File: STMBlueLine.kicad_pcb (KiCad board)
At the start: 2 copper layers, 22 x 42 mm, 80 parts, among them J1 Micro_SD_Card_Det1, J2 USB_C_Receptacle_USB2.0_14P, J3 Conn_01x04_Pin, SW1 SW_Push, SW2 SW_Push, U1 STM32H750VBTx, U2 TLV320AIC3104IRHBR, U3 TLV320AIC3104IRHBR, U4 LD1117S33TR_SOT223, U5 USBLC6-2SC6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

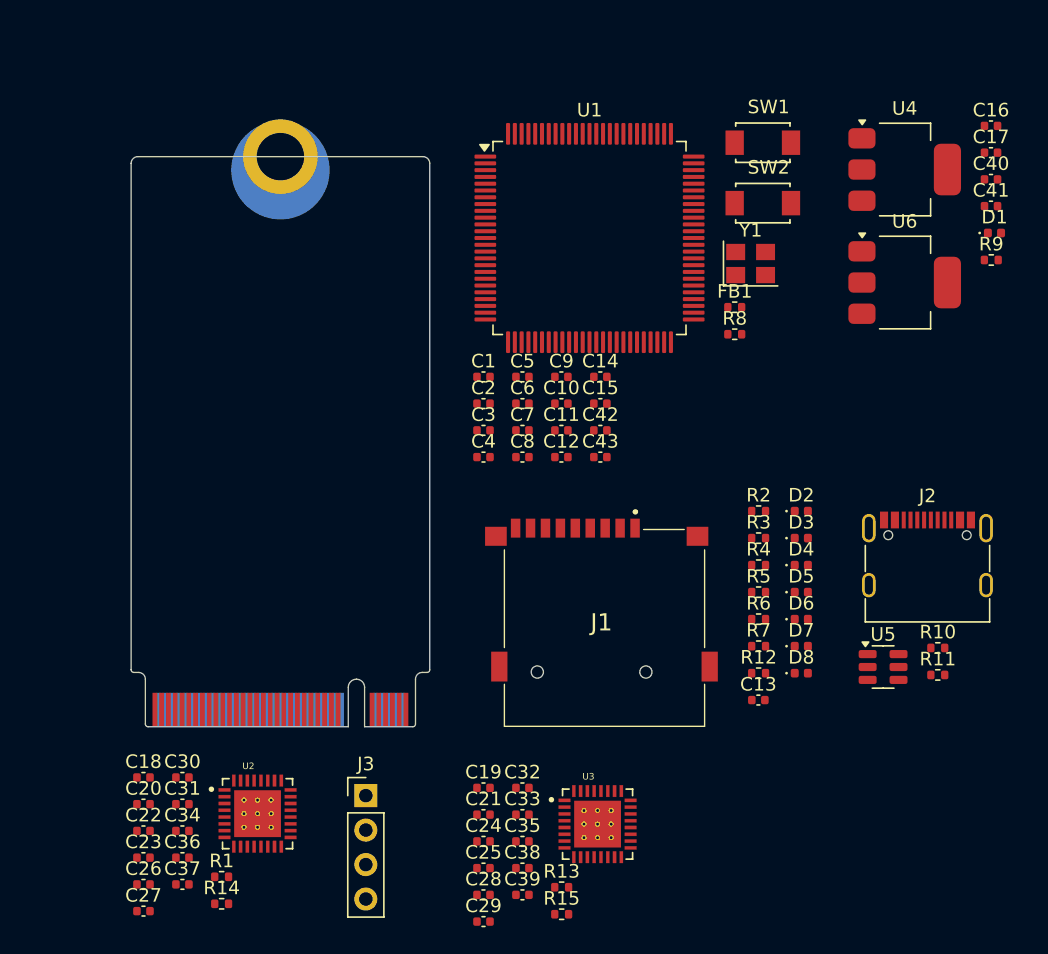
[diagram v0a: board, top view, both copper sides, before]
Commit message: ADD : Rough PCB part placement. MOD : Swapped codec DVDD LDO.
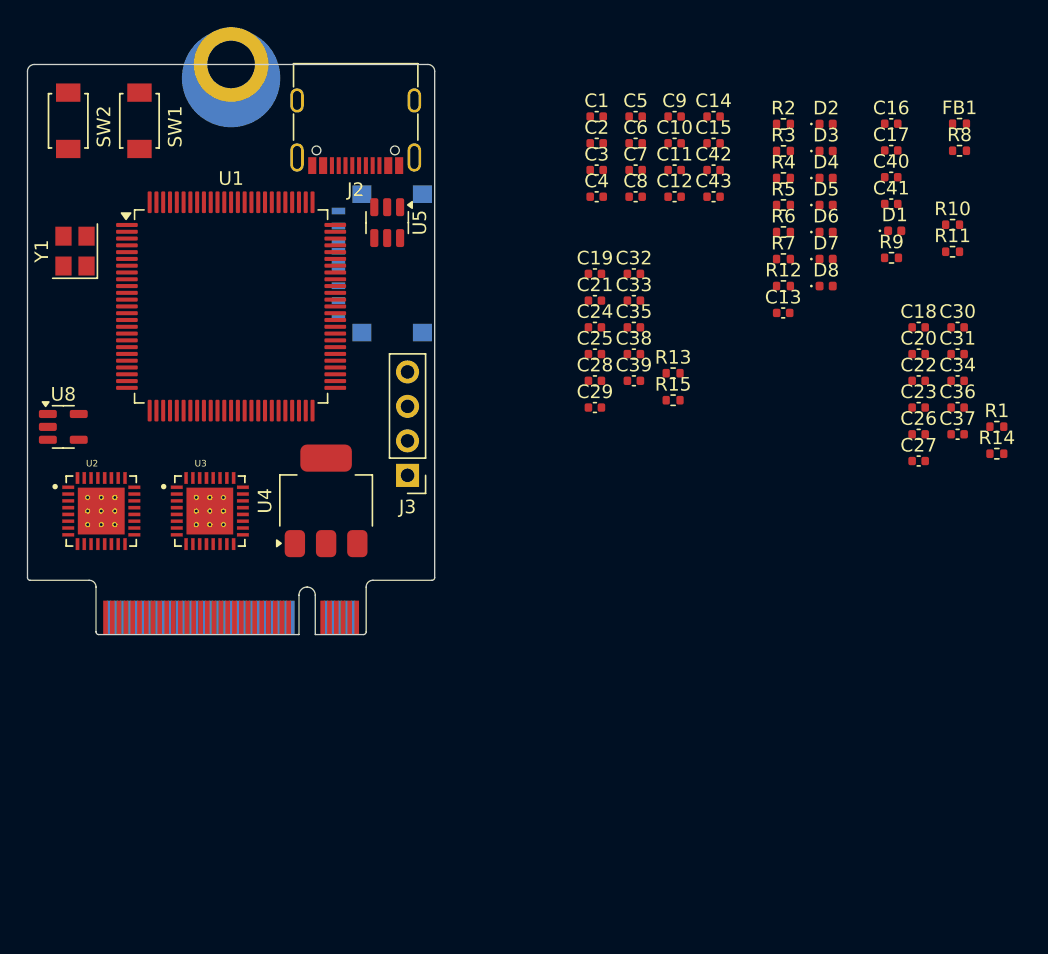
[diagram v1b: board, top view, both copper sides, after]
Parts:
- removed U6: LD1117S18TR_SOT223, Package_TO_SOT_SMD:SOT-223-3_TabPin2
- added U8: TLV74333PDBVR_SOT23-5, Package_TO_SOT_SMD:SOT-23-5, F.Cu at (19.3, 43.4)
- J1: footprint random-footprints:TF15X15 -> easyeda2kicad:TF-SMD_TF-123-ARP9H15; moved to B.Cu
- moved C18 66.0 mm to (82.3, 36.0)
- moved C20 66.0 mm to (82.3, 38.0)
- moved C22 66.0 mm to (82.3, 40.0)
- moved C23 66.0 mm to (82.3, 42.0)
- moved C26 66.0 mm to (82.3, 43.9)
- moved C27 66.0 mm to (82.3, 45.9)
- moved C30 66.0 mm to (85.2, 36.0)
- moved C31 66.0 mm to (85.2, 38.0)
- moved C34 66.0 mm to (85.2, 40.0)
- moved C36 66.0 mm to (85.2, 42.0)
- moved C37 66.0 mm to (85.2, 43.9)
- moved R1 66.0 mm to (88.1, 43.4)
- moved R14 66.0 mm to (88.1, 45.4)
- moved J2 53.9 mm to (40.9, 20.4), turned to 180 degrees
- moved SW2 51.5 mm to (19.7, 20.8), turned to -90 degrees
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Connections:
- C26 pad 1: GND -> GNDA
- C27 pad 1: GND -> GNDA
- C28 pad 1: GND -> GNDA
- C29 pad 1: GND -> GNDA
- C30 pad 1: GND -> GNDA
- C31 pad 1: GND -> GNDA
- C32 pad 1: GND -> GNDA
- C33 pad 1: GND -> GNDA
- C34 pad 1: GND -> GNDA
- C35 pad 1: GND -> GNDA
- C36 pad 1: GND -> GNDA
- C37 pad 1: GND -> GNDA
- C38 pad 1: GND -> GNDA
- C39 pad 1: GND -> GNDA
- U2 pad 17: GND -> GNDA
- U2 pad 21: GND -> GNDA
- U2 pad 26: GND -> GNDA
- U2 pad 33: GND -> GNDA
- U2 pad 33_1: GND -> GNDA
- U2 pad 33_2: GND -> GNDA
- U2 pad 33_3: GND -> GNDA
- U2 pad 33_4: GND -> GNDA
- U2 pad 33_5: GND -> GNDA
- U2 pad 33_6: GND -> GNDA
- U2 pad 33_7: GND -> GNDA
- U2 pad 33_8: GND -> GNDA
- U2 pad 33_9: GND -> GNDA
- U3 pad 17: GND -> GNDA
- U3 pad 21: GND -> GNDA
- U3 pad 26: GND -> GNDA
- U3 pad 33: GND -> GNDA
- U3 pad 33_1: GND -> GNDA
- U3 pad 33_2: GND -> GNDA
- U3 pad 33_3: GND -> GNDA
- U3 pad 33_4: GND -> GNDA
- U3 pad 33_5: GND -> GNDA
- U3 pad 33_6: GND -> GNDA
- U3 pad 33_7: GND -> GNDA
- U3 pad 33_8: GND -> GNDA
- U3 pad 33_9: GND -> GNDA
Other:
- board size 22 x 42 mm -> 30 x 42 mm

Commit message: ADD : PCB Stackup
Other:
- copper layers 2 -> 4
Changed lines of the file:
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@@
 	(generator_version "9.0")
 	(general
-		(thickness 1.6)
+		(thickness 0.8192)
 		(legacy_teardrops no)
 	)
@@
 	(layers
 		(0 "F.Cu" signal)
+		(4 "In1.Cu" signal)
+		(6 "In2.Cu" signal)
 		(2 "B.Cu" signal)
 		(9 "F.Adhes" user "F.Adhesive")
@@
 	)
 	(setup
+		(stackup
+			(layer "F.SilkS"
+				(type "Top Silk Screen")
+				(color "White")
+			)
+			(layer "F.Paste"
+				(type "Top Solder Paste")
+			)
+			(layer "F.Mask"
+				(type "Top Solder Mask")
+				(color "Green")
+				(thickness 0.01)
+			)
+			(layer "F.Cu"
+				(type "copper")
+				(thickness 0.035)
+			)
+			(layer "dielectric 1"
+				(type "prepreg")
+				(color "FR4 natural")
+				(thickness 0.0994)
+				(material "FR4")
+				(epsilon_r 4.5)
+				(loss_tangent 0.02)
+			)
+			(layer "In1.Cu"
+				(type "copper")
+				(thickness 0.0152)
+			)
+			(layer "dielectric 2"
+				(type "core")
+				(color "FR4 natural")
+				(thickness 0.5)
+				(material "FR4")
+				(epsilon_r 4.5)
+				(loss_tangent 0.02)
+			)
+			(layer "In2.Cu"
+				(type "copper")
+				(thickness 0.0152)
+			)
+			(layer "dielectric 3"
+				(type "prepreg")
+				(color "FR4 natural")
+				(thickness 0.0994)
+				(material "FR4")
+				(epsilon_r 4.5)
+				(loss_tangent 0.02)
+			)
+			(layer "B.Cu"
+				(type "copper")
+				(thickness 0.035)
+			)
+			(layer "B.Mask"
+				(type "Bottom Solder Mask")
+				(color "Green")
+				(thickness 0.01)
+			)
+			(layer "B.Paste"
+				(type "Bottom Solder Paste")
+			)
+			(layer "B.SilkS"
+				(type "Bottom Silk Screen")
+				(color "White")
+			)
+			(copper_finish "None")
+			(dielectric_constraints no)
+		)
 		(pad_to_mask_clearance 0)
 		(allow_soldermask_bridges_in_footprints no)
@@
 		(embedded_fonts no)
 	)
-	(embedded_fonts no)
+	(embedded_fonts yes)
 )
